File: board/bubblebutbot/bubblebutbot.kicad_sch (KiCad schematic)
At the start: 55 parts, among them J1 JST XH, J10 JST XH, J11 JST XH, J13 JST XH, J2 USB_C_Receptacle, J3 Conn_01x03_Socket, J4 Conn_01x03_Socket, J5 Conn_01x03_Socket, J6 Conn_01x03_Socket, J7 Conn_01x03_Socket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

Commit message: pcb done!
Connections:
- net 5V_SUPPLY is gone; now on net +5V: C8.2, R11.1, U1.12 (VM)
- net ESP32-ACC-INT1: now also U2.22 (GPIO14/TOUCH14/ADC2_CH3/FSPIWP/FSPIDQS/SUBSPIWP); no longer U2.24 (GPIO47/SPICLK_P/SUBSPICLK_P_DIFF)
- net ESP32-ACC-INT2: now also U2.23 (GPIO21); no longer U2.25 (GPIO48/SPICLK_N/SUBSPICLK_N_DIFF)
- net ESP32-ACC-SCL: now also U2.25 (GPIO48/SPICLK_N/SUBSPICLK_N_DIFF); no longer U2.21 (GPIO13/TOUCH13/ADC2_CH2/FSPIQ/FSPIIO7/SUBSPIQ)
- net ESP32-ACC-SDA: now also U2.24 (GPIO47/SPICLK_P/SUBSPICLK_P_DIFF); no longer U2.20 (GPIO12/TOUCH12/ADC2_CH1/FSPICLK/FSPIIO6/SUBSPICLK)
- net ESP32-IR-BL: now also U2.5 (GPIO5/TOUCH5/ADC1_CH4); no longer U2.6 (GPIO6/TOUCH6/ADC1_CH5)
- net ESP32-IR-BR: now also U2.4 (GPIO4/TOUCH4/ADC1_CH3); no longer U2.7 (GPIO7/TOUCH7/ADC1_CH6)
- net ESP32-IR-FL: now also U2.7 (GPIO7/TOUCH7/ADC1_CH6); no longer U2.4 (GPIO4/TOUCH4/ADC1_CH3)
- net ESP32-IR-FR: now also U2.6 (GPIO6/TOUCH6/ADC1_CH5); no longer U2.5 (GPIO5/TOUCH5/ADC1_CH4)
- net ESP32-MOTOR-AIN1: now also U2.17 (GPIO9/TOUCH9/ADC1_CH8/FSPIHD/SUBSPIHD); no longer U2.10 (GPIO17/U1TXD/ADC2_CH6)
- net ESP32-MOTOR-AIN2: now also U2.18 (GPIO10/TOUCH10/ADC1_CH9/FSPICS0/FSPIIO4/SUBSPICS0); no longer U2.11 (GPIO18/U1RXD/ADC2_CH7/CLK_OUT3)
- net ESP32-MOTOR-BIN1: now also U2.19 (GPIO11/TOUCH11/ADC2_CH0/FSPID/FSPIIO5/SUBSPID); no longer U2.23 (GPIO21)
- net ESP32-MOTOR-FAULT: now also U2.20 (GPIO12/TOUCH12/ADC2_CH1/FSPICLK/FSPIIO6/SUBSPICLK); no longer U2.22 (GPIO14/TOUCH14/ADC2_CH3/FSPIWP/FSPIDQS/SUBSPIWP)
- net ESP32-OP-LED: now also U2.21 (GPIO13/TOUCH13/ADC2_CH2/FSPIQ/FSPIIO7/SUBSPIQ); no longer U2.19 (GPIO11/TOUCH11/ADC2_CH0/FSPID/FSPIIO5/SUBSPID)
- net ESP32-SRV-B: now also U2.10 (GPIO17/U1TXD/ADC2_CH6); no longer U2.17 (GPIO9/TOUCH9/ADC1_CH8/FSPIHD/SUBSPIHD)
- net ESP32-SRV-F: now also U2.11 (GPIO18/U1RXD/ADC2_CH7/CLK_OUT3); no longer U2.18 (GPIO10/TOUCH10/ADC1_CH9/FSPICS0/FSPIIO4/SUBSPICS0)

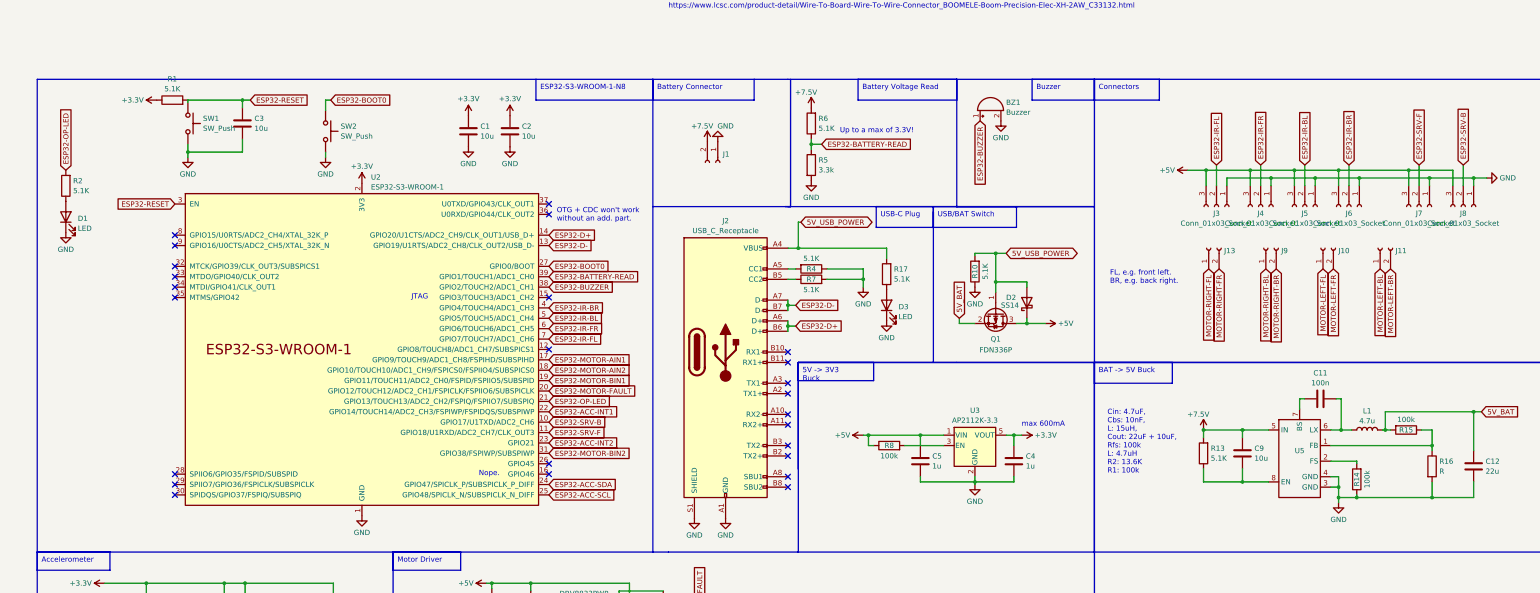
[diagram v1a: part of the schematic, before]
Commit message: support for esp32s3
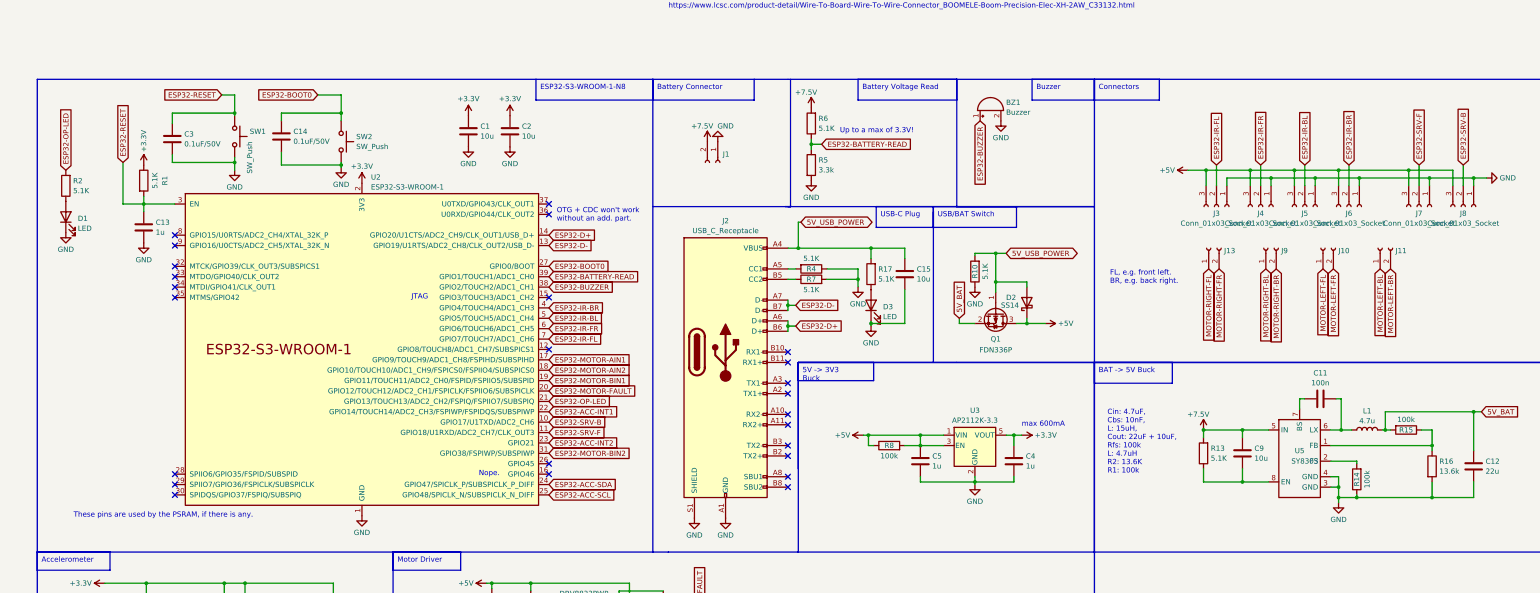
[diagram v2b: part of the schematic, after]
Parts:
- added C13: 1u, Capacitor_SMD:C_0603_1608Metric_Pad1.08x0.95mm_HandSolder, symbol Device:C
- added C14: 0.1uF/50V, symbol Device:C
- added C15: 10u, Capacitor_SMD:C_0603_1608Metric_Pad1.08x0.95mm_HandSolder, symbol Device:C
- C3: value 10u -> 0.1uF/50V; footprint Capacitor_SMD:C_0603_1608Metric_Pad1.08x0.95mm_HandSolder -> (none); LCSC C380316 -> (none)
- R16: value R -> 13.6k
- U5: value ~ -> SY8303
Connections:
- net +5V: now also R8.2, U3.3 (EN)
- net 5V_USB_POWER: now also C15.1
- net ESP32-BOOT0: now also C14.1
- net ESP32-RESET: now also C13.1
- net GND: now also C13.2, C14.2, C15.2
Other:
- note added: "These pins are used by the PSRAM, if there is any."
- moved on the sheet: D3, R1, R17, SW1, SW2

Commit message: a few comments
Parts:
- removed R13: 5.1K, Resistor_SMD:R_0603_1608Metric_Pad0.98x0.95mm_HandSolder, symbol Device:R
- added C16: 10u, Capacitor_SMD:C_0603_1608Metric_Pad1.08x0.95mm_HandSolder, symbol Device:C
- added R3: 100k, Resistor_SMD:R_0603_1608Metric_Pad0.98x0.95mm_HandSolder, symbol Device:R
- added SW3: SW_SPDT, Button_Switch_THT:SW_Slide_1P2T_CK_OS102011MS2Q, symbol Switch:SW_SPDT
- C11: value 100n -> 10n; LCSC C282519 -> C525264
- C9: LCSC C380316 -> C7393897
- SW1, SW2: footprint Button_Switch_SMD:SW_SPST_B3U-1000P -> Button_Switch_THT:SW_PUSH_6mm_H4.3mm; LCSC C455280 -> (none)
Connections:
- net +5V: now also J7.2 (Pin_2), J8.2 (Pin_2), C16.1, SW3.3 (C); no longer D2.1 (K), J7.3 (Pin_3), J8.3 (Pin_3), Q1.3 (D)
- net +7.5V: now also R3.2
- net ESP32-SRV-B: now also J8.3 (Pin_3); no longer J8.2 (Pin_2)
- net ESP32-SRV-F: now also J7.3 (Pin_3); no longer J7.2 (Pin_2)
- net GND: now also C16.2
- net at C9.2, U5.8 (EN): now also R3.1
- new net 5V_SPLY: D2.1 (K), Q1.3 (D), SW3.2 (B)
- no-connect marks 29 -> 30

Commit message: pcb 1v04
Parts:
- removed BZ1: Buzzer, Buzzer_Beeper:MagneticBuzzer_PUI_AT-0927-TT-6-R, symbol Device:Buzzer
- removed C15: 10u, Capacitor_SMD:C_0603_1608Metric_Pad1.08x0.95mm_HandSolder, symbol Device:C
- removed J5, J6, J8: Conn_01x03_Socket, Connector_JST:JST_PH_S3B-PH-K_1x03_P2.00mm_Horizontal, symbol Connector:Conn_01x03_Socket
- removed SW3: SW_SPDT, Button_Switch_THT:SW_Slide_1P2T_CK_OS102011MS2Q, symbol Switch:SW_SPDT
- added D4: SS14, Diode_SMD:D_SMA, symbol Device:D_Schottky
- added J5, J6: Conn_01x01_Pin, TestPoint:TestPoint_Pad_2.0x2.0mm, symbol Connector:Conn_01x01_Pin
- C14, C3: footprint (none) -> Capacitor_SMD:C_0603_1608Metric_Pad1.08x0.95mm_HandSolder
- C16: value 10u -> 22u; footprint Capacitor_SMD:C_0603_1608Metric_Pad1.08x0.95mm_HandSolder -> Capacitor_SMD:C_1206_3216Metric_Pad1.33x1.80mm_HandSolder; LCSC C7393897 -> C12891
- R11: value 50k -> 100k; LCSC C304067 -> C2907088
- R16: value 13.6k -> 12k; LCSC C2930064 -> C2907097
- SW1, SW2: footprint Button_Switch_THT:SW_PUSH_6mm_H4.3mm -> Button_Switch_SMD:SW_SPST_CK_RS282G05A3
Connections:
- net 5V_SPLY is gone; now on net +5V: D2.1 (K), Q1.3 (D)
- net ESP32-SRV-B is gone; now on net ESP32-SRV-F: U2.10 (GPIO17/U1TXD/ADC2_CH6)
- net +5V: now also R11.2; no longer C16.1, R11.1, R8.2, U3.3 (EN)
- net +7.5V: now also J5.1 (Pin_1); no longer C9.1, R3.2, R6.2, U5.5 (IN)
- net 5V_BAT: now also D4.1 (K); no longer C12.1, L1.2, R15.2
- net ESP32-IR-FL: now also U2.12 (GPIO8/TOUCH8/ADC1_CH7/SUBSPICS1); no longer U2.7 (GPIO7/TOUCH7/ADC1_CH6)
- net ESP32-IR-FR: now also U2.11 (GPIO18/U1RXD/ADC2_CH7/CLK_OUT3); no longer U2.6 (GPIO6/TOUCH6/ADC1_CH5)
- net ESP32-SRV-F: now also J7.1 (Pin_1); no longer J7.3 (Pin_3), U2.11 (GPIO18/U1RXD/ADC2_CH7/CLK_OUT3)
- net GND: now also J7.3 (Pin_3); no longer J7.1 (Pin_1)
- net at U1.1 (nSLEEP): now also R11.1; no longer R11.2
- net ESP32-BUZZER: no longer names the net of U2.38 (GPIO2/TOUCH2/ADC1_CH1)
- net ESP32-IR-BL: no longer names the net of U2.5 (GPIO5/TOUCH5/ADC1_CH4)
- net ESP32-IR-BR: no longer names the net of U2.4 (GPIO4/TOUCH4/ADC1_CH3)
- new net: C12.1, D4.2 (A), L1.2, R15.2
- new net: R8.2, U3.3 (EN)
- new net BAT_OUT: C16.1, C9.1, J6.1 (Pin_1), R3.2, R6.2, U5.5 (IN)
- no-connect marks 30 -> 33
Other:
- note added: "VOUT=0.6*(1+R1/R2)"
- note added: "We aim for 5.5V"
- note added: "We assume a 500mV drop"
- note added: "power switch before the buck converter, close to the battery."
- moved on the sheet: C5, D2, D3, Q1, R10, R17, R8

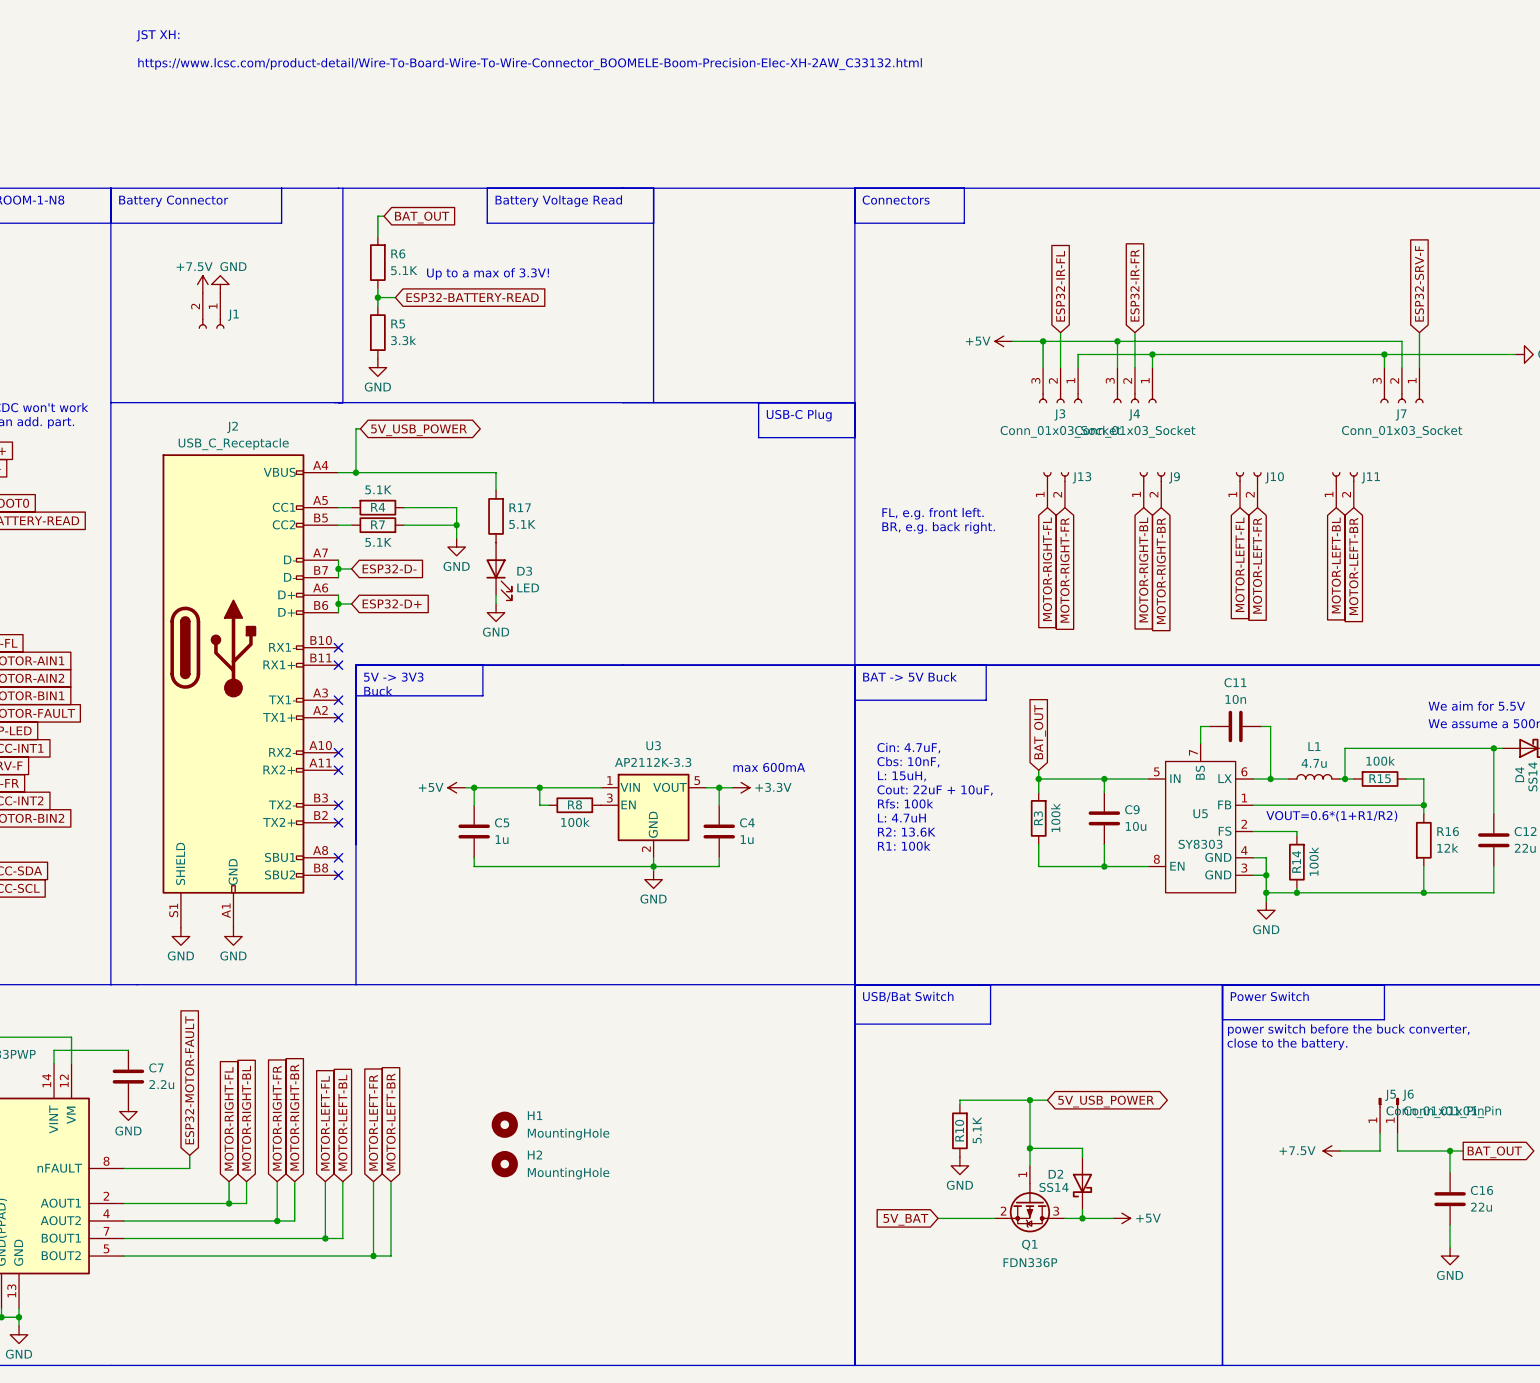
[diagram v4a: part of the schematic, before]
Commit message: pcb v0.5
smaller
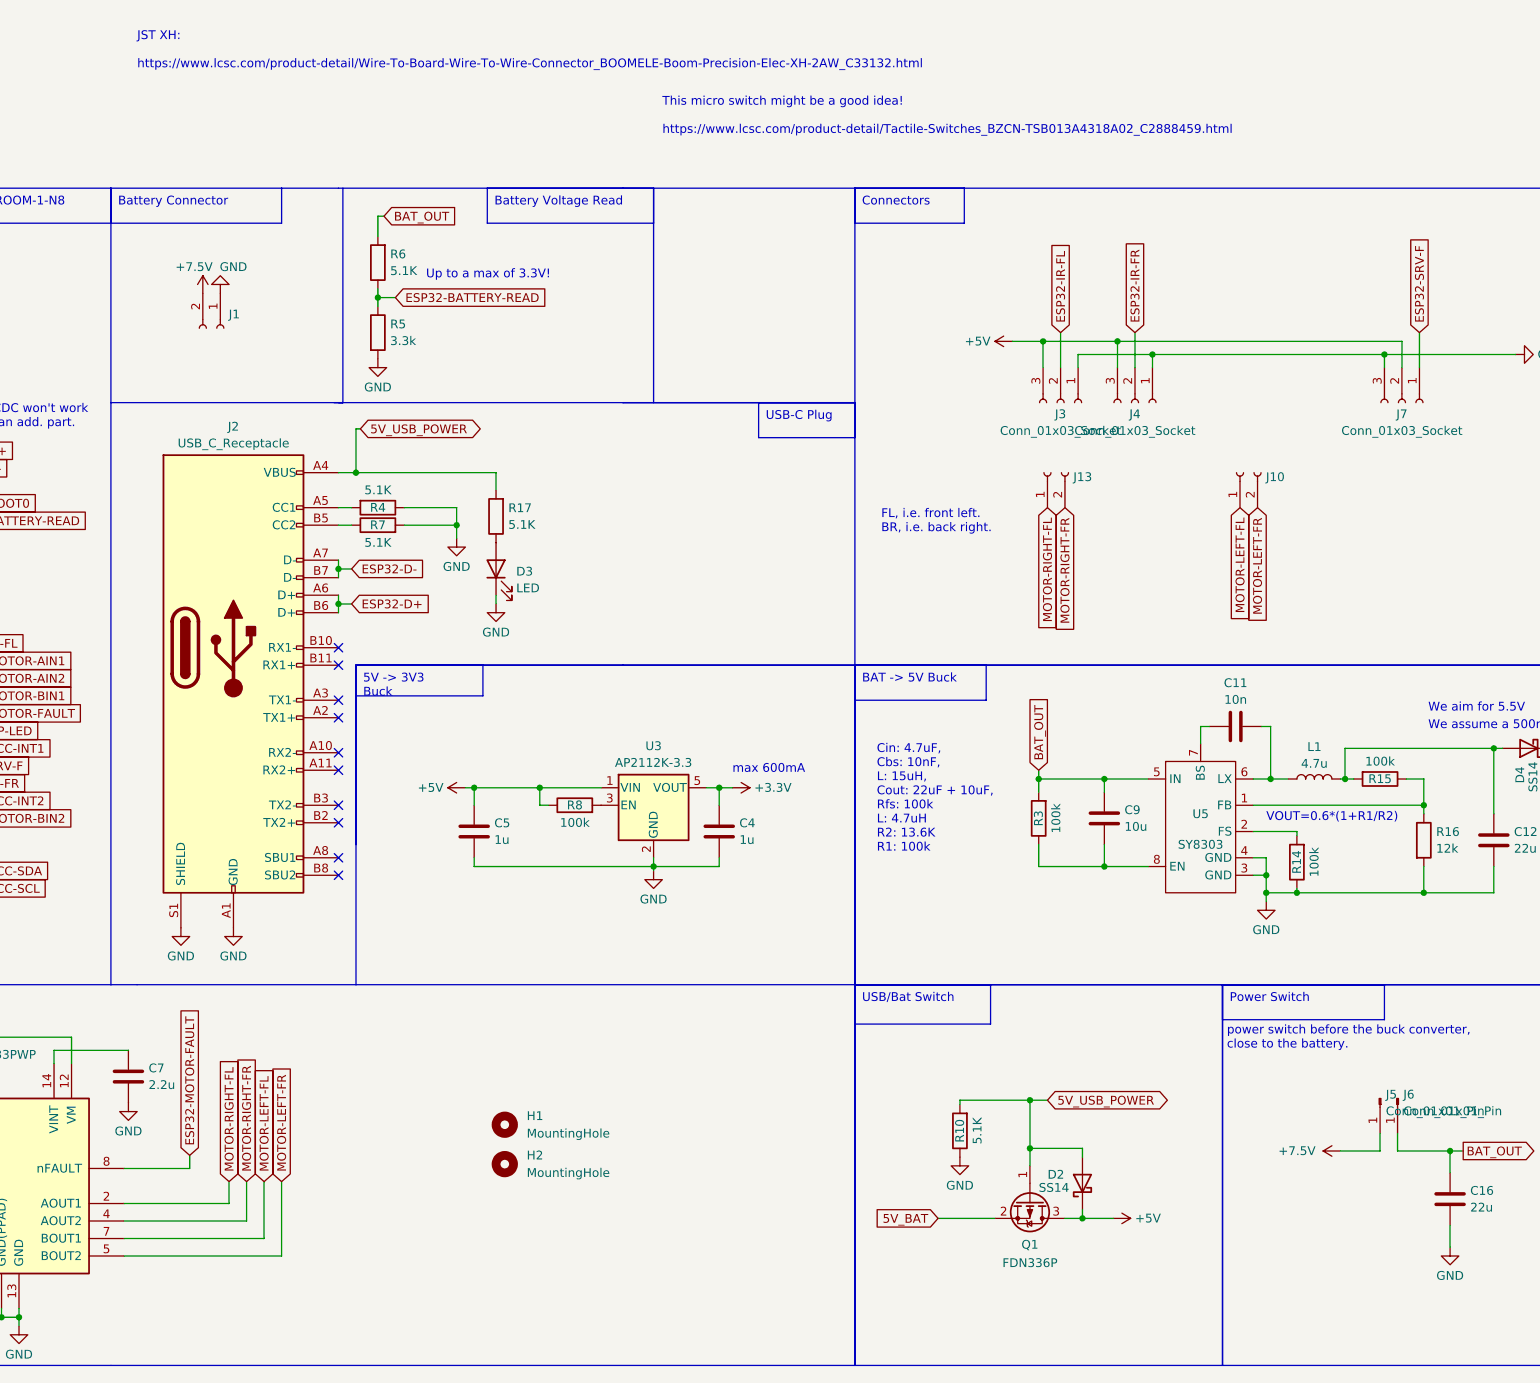
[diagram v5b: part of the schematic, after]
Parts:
- removed J11, J9: JST XH, Connector_JST:JST_PH_S2B-PH-K_1x02_P2.00mm_Horizontal, symbol Connector:Conn_01x02_Socket
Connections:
- net MOTOR-LEFT-BL renamed MOTOR-LEFT-FL
- net MOTOR-LEFT-BR renamed MOTOR-LEFT-FR
- net MOTOR-RIGHT-BL renamed MOTOR-RIGHT-FL
- net MOTOR-RIGHT-BR renamed MOTOR-RIGHT-FR
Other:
- note added: "FL, i.e. front left. BR, i.e. back right."
- note added: "This micro switch might be a good idea! https://www.lcsc.com/product-detail/Tactile-Switches_BZCN-TSB013A4318A02_C2888459.html"
- note removed: "FL, e.g. front left. BR, e.g. back right."

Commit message: v2.06 schamtic
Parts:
- removed C12: 22u, Capacitor_SMD:C_1206_3216Metric_Pad1.33x1.80mm_HandSolder, symbol Device:C
- removed Q1: FDN336P, Package_TO_SOT_SMD:SOT-23, symbol Transistor_FET:FDN340P
- removed R10: 5.1K, Resistor_SMD:R_0603_1608Metric_Pad0.98x0.95mm_HandSolder, symbol Device:R
- removed R14, R15, R3, R8: 100k, Resistor_SMD:R_0603_1608Metric_Pad0.98x0.95mm_HandSolder, symbol Device:R
- removed R16: 12k, Resistor_SMD:R_0603_1608Metric_Pad0.98x0.95mm_HandSolder, symbol Device:R
- removed U3: AP2112K-3.3, Package_TO_SOT_SMD:SOT-23-5, symbol Regulator_Linear:AP2112K-3.3
- removed U5: SY8303, Package_TO_SOT_SMD:SOT-23-8, symbol CustomSymbols:SY8303
- added U3: AP63203WU, Package_TO_SOT_SMD:TSOT-23-6, symbol Regulator_Switching:AP63203WU
- C11: value 10n -> 100n; LCSC C525264 -> C282519
- C4, C5: value 1u -> 22u; footprint Capacitor_SMD:C_0603_1608Metric_Pad1.08x0.95mm_HandSolder -> Capacitor_SMD:C_1206_3216Metric_Pad1.33x1.80mm_HandSolder; LCSC C1592 -> C12891
- C9: LCSC C7393897 -> C380316
- L1: value 4.7u -> 3.3u; footprint Inductor_SMD:L_Wuerth_WE-TPC-3816 -> Inductor_SMD:L_Wuerth_WE-PD2-Typ-MS; LCSC C2879693 -> C2929417
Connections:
- net 5V_BAT is gone; now on net BAT_OUT: D4.1 (K)
- net +3.3V: no longer C4.1
- net +5V: no longer C5.1, C8.2, D2.1 (K), R11.2, U1.12 (VM)
- net BAT_OUT: now also C8.2, D2.1 (K), R11.2, U1.12 (VM), U3.2 (EN), U3.3 (IN); no longer C16.1, J6.1 (Pin_1), R6.2
- net GND: now also C9.2, U3.4 (GND)
- net at L1.2: now also C4.1, C5.1, U3.1 (FB); no longer D4.2 (A)
- net at C11.1: now also L1.1, U3.5 (SW)
- net at C11.2: now also U3.6 (BST); no longer L1.1
- new net BAT_IN: C16.1, D4.2 (A), J6.1 (Pin_1), R6.2
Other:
- note added: "Dual Diode approach will suffice for now. Later I'll look into a better circuit. The Vdrop is about 0.4V"
- note added: "Recommended is 3.9uH!"
- note added: "Vgs (NO USB) = -8.4V (BAT ON) Vgs (USB) = 5 - 8.4 = -3.4V (BAT Part ON) I need a PNP with a Vgsth > -3.4V"
- note removed: "Cin: 4.7uF, Cbs: 10nF, L: 15uH, Cout: 22uF + 10uF, Rfs: 100k L: 4.7uH R2: 13.6K R1: 100k"
- note removed: "VOUT=0.6*(1+R1/R2)"
- note removed: "We aim for 5.5V"
- note removed: "We assume a 500mV drop"
- note removed: "max 600mA"
- moved on the sheet: D2
